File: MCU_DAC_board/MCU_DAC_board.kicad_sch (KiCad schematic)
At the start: 39 parts, among them J10 Screw_Terminal_01x02, J11 105-0752-001, J5 54-00127, J6 105-0752-001, J7 Screw_Terminal_01x02, J8 Screw_Terminal_01x02, J9 Screw_Terminal_01x02, Q1 FZT953, U1 ADAU1966AWBSTZ, U2 ESP32-S3-DEVKITC-1-N8R2

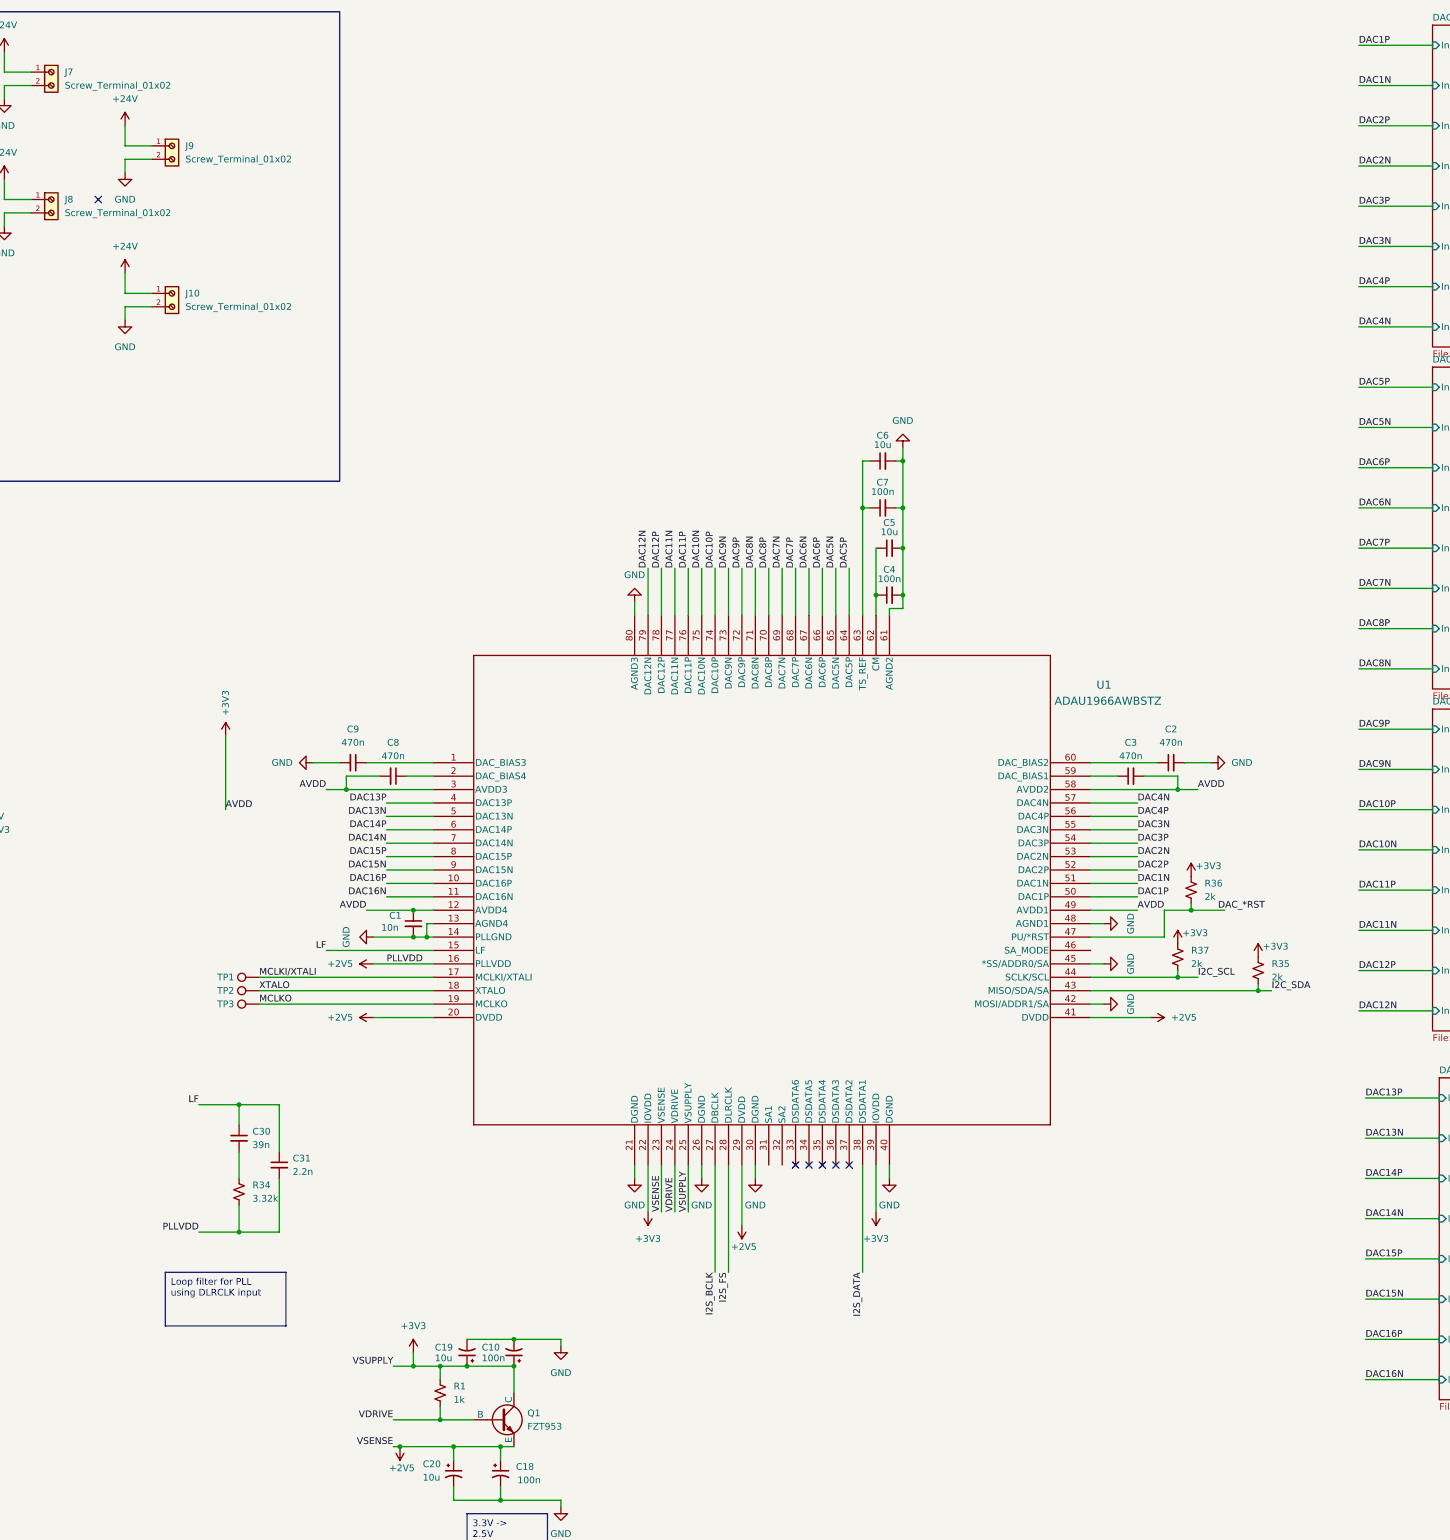
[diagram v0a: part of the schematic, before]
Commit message: Finished layout for DAC board with 1 MCU
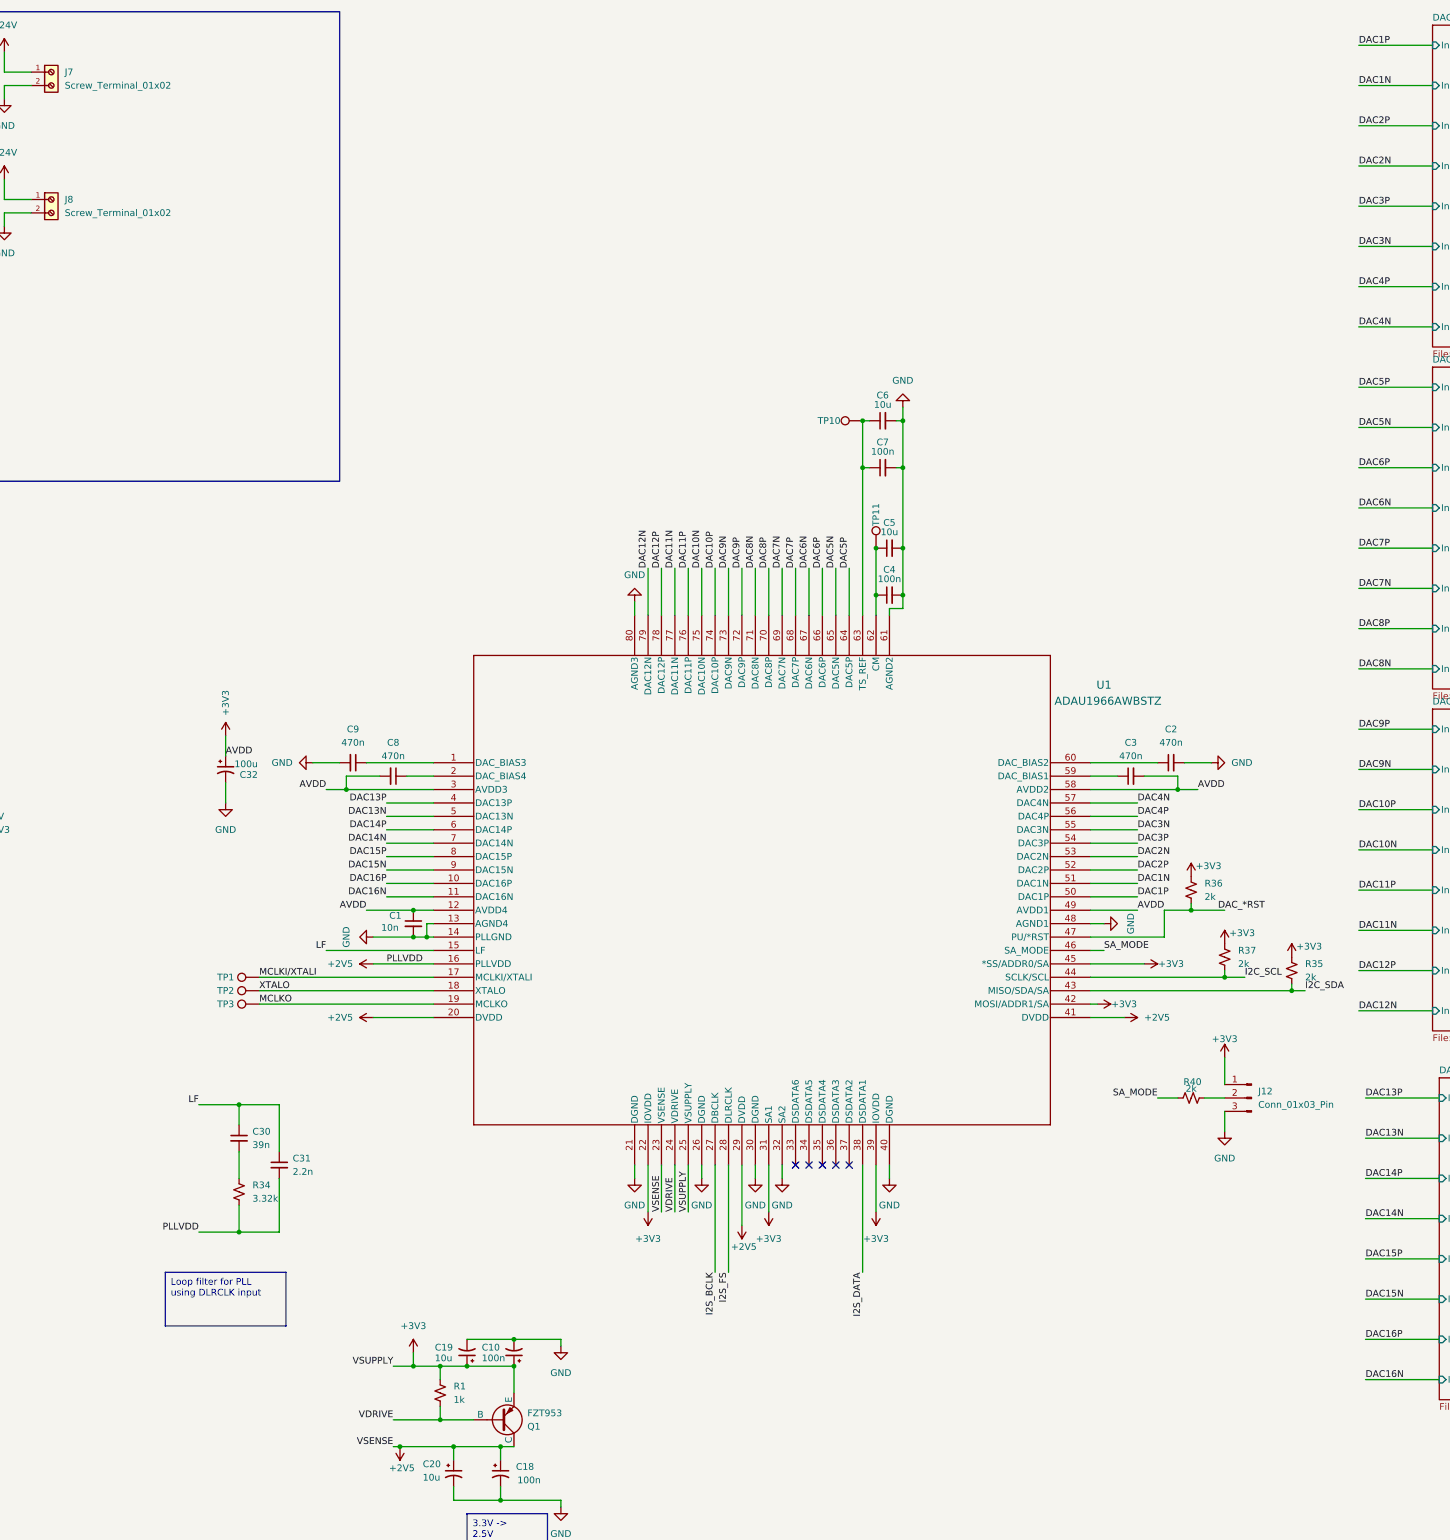
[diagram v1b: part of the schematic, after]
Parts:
- removed J10, J9: Screw_Terminal_01x02, project_lib:691137710002, symbol project_lib:691137710002
- added C32: 100u, Capacitor_THT:CP_Radial_D6.3mm_P2.50mm, symbol Device:C_Polarized_Small_US
- added J12: Conn_01x03_Pin, Connector_PinHeader_2.54mm:PinHeader_1x03_P2.54mm_Vertical, symbol Connector:Conn_01x03_Pin
- added R40: 2k, Resistor_SMD:R_0805_2012Metric_Pad1.20x1.40mm_HandSolder, symbol Device:R_Small_US
- added TP10: TS_REF, project_lib:TP_1.8x1mm, symbol Connector:TestPoint
- added TP11: CM, project_lib:TP_1.8x1mm, symbol Connector:TestPoint
- Q1: symbol Simulation_SPICE:NPN -> Simulation_SPICE:PNP
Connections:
- net +2V5: now also Q1.1 (C); no longer Q1.3 (E)
- net +3V3: now also Q1.3 (E), U1.31 (SA1), U1.42 (MOSI/ADDR1/SA), U1.45 (*SS/ADDR0/SA), C32.1, J12.1 (Pin_1); no longer Q1.1 (C)
- net GND: now also U1.32 (SA2), C32.2, J12.3 (Pin_3); no longer U1.42 (MOSI/ADDR1/SA), U1.45 (*SS/ADDR0/SA)
- net SA_MODE: now reaches U1.46 (SA_MODE)
- net SA_MODE: now also R40.1
- net at C4.1, C5.1, U1.62 (CM): now also TP11.1
- net at C6.1, C7.1, U1.63 (TS_REF): now also TP10.1
- new net: J12.2 (Pin_2), R40.2
- no-connect marks 6 -> 5
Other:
- moved on the sheet: C6, C7, R35, R37

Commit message: did a thing
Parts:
- added U3: ESP32-S3-DEVKITC-1-N8R2, project_lib:XCVR_ESP32-S3-DEVKITC-1-N8R2, symbol project_lib:ESP32-S3-DEVKITC-1-N8R2
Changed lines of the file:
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@@
+	)
+	(symbol
+		(lib_id "project_lib:ESP32-S3-DEVKITC-1-N8R2")
+		(at 91.44 331.47 0)
+		(unit 1)
+		(exclude_from_sim no)
+		(in_bom yes)
+		(on_board yes)
+		(dnp no)
+		(fields_autoplaced yes)
+		(property "Reference" "U3"
+			(at 91.44 293.37 0)
+			(effects
+				(font
+					(size 1.27 1.27)
+				)
+			)
+		)
+		(property "Value" "ESP32-S3-DEVKITC-1-N8R2"
+			(at 91.44 295.91 0)
+			(effects
+				(font
+					(size 1.27 1.27)
+				)
+			)
+		)
+		(property "Footprint" "project_lib:XCVR_ESP32-S3-DEVKITC-1-N8R2"
+			(at 91.44 331.47 0)
+			(effects
+				(font
+					(size 1.27 1.27)
+				)
+				(justify bottom)
+				(hide yes)
+			)
+		)
+		(property "Datasheet" ""
+			(at 91.44 331.47 0)
+			(effects
+				(font
+					(size 1.27 1.27)
+				)
+				(hide yes)
+			)
+		)
+		(property "Description" ""
+			(at 91.44 331.47 0)
+			(effects
+				(font
+					(size 1.27 1.27)
+				)
+				(hide yes)
+			)
+		)
+		(property "PARTREV" "V1"
+			(at 91.44 331.47 0)
+			(effects
+				(font
+					(size 1.27 1.27)
+				)
+				(justify bottom)
+				(hide yes)
+			)
+		)
+		(property "STANDARD" "Manufacturer Recommendations"
+			(at 91.44 331.47 0)
+			(effects
+				(font
+					(size 1.27 1.27)
+				)
+				(justify bottom)
+				(hide yes)
+			)
+		)
+		(property "MANUFACTURER" "Espressif"
+			(at 91.44 331.47 0)
+			(effects
+				(font
+					(size 1.27 1.27)
+				)
+				(justify bottom)
+				(hide yes)
+			)
+		)
+		(pin "J1_3"
+		)
+		(pin "J1_6"
+		)
+		(pin "J1_1"
+		)
+		(pin "J1_18"
+		)
+		(pin "J1_7"
+		)
+		(pin "J1_2"
+		)
+		(pin "J3_11"
+		)
+		(pin "J1_17"
+		)
+		(pin "J3_13"
+		)
+		(pin "J3_12"
+		)
+		(pin "J3_10"
+		)
+		(pin "J1_22"
+		)
+		(pin "J1_21"
+		)
+		(pin "J3_5"
+		)
+		(pin "J3_16"
+		)
+		(pin "J1_5"
+		)
+		(pin "J1_15"
+		)
+		(pin "J1_16"
+		)
+		(pin "J3_17"
+		)
+		(pin "J3_14"
+		)
+		(pin "J1_20"
+		)
+		(pin "J3_1"
+		)
+		(pin "J3_18"
+		)
+		(pin "J3_6"
+		)
+		(pin "J3_3"
+		)
+		(pin "J3_21"
+		)
+		(pin "J1_10"
+		)
+		(pin "J1_19"
+		)
+		(pin "J3_20"
+		)
+		(pin "J1_9"
+		)
+		(pin "J3_9"
+		)
+		(pin "J3_7"
+		)
+		(pin "J3_8"
+		)
+		(pin "J1_14"
+		)
+		(pin "J1_8"
+		)
+		(pin "J3_2"
+		)
+		(pin "J3_19"
+		)
+		(pin "J3_22"
+		)
+		(pin "J1_13"
+		)
+		(pin "J3_4"
+		)
+		(pin "J1_4"
+		)
+		(pin "J1_11"
+		)
+		(pin "J3_15"
+		)
+		(pin "J1_12"
+		)
+		(instances
+			(project "MCU_DAC_board"
+				(path "/04313b52-c86e-4005-b50d-74ee3e5645b2"
+					(reference "U3")
+					(unit 1)
+				)
+			)
+		)
 	)
 	(symbol
